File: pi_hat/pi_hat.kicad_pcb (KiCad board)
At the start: 2 copper layers, 65 x 56.5 mm, 47 parts, among them J1 Conn_Coaxial, J2 Conn_Coaxial, J3 Conn_02x20_Odd_Even, J4 Conn_02x04_Odd_Even, J5 Conn_02x02_Odd_Even, T1 2873002402, T2 2873002402, U1 FOX924, U2 Si5351A-B-GM, U3 FST3253, U4 FST3253, U5 TLV320ADC5140, U6 CAT24C32

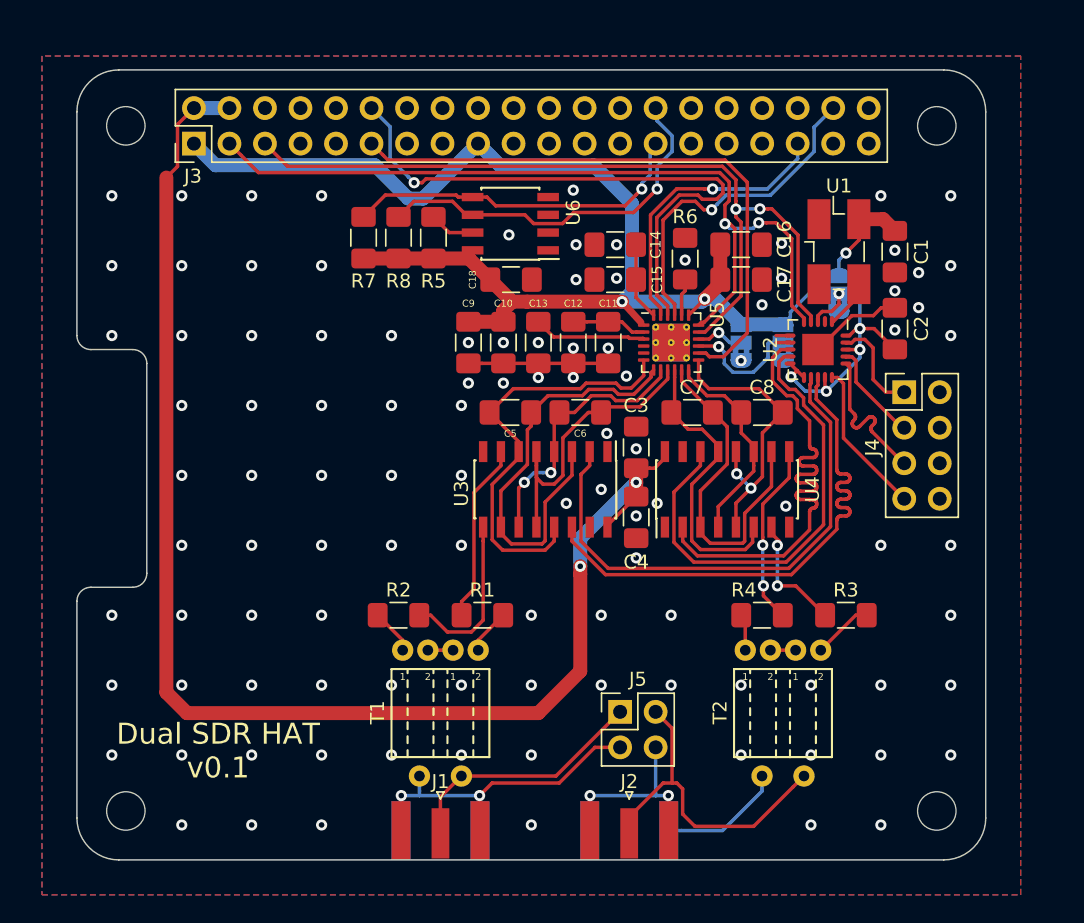
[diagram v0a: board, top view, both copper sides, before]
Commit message: Add header for external filter board
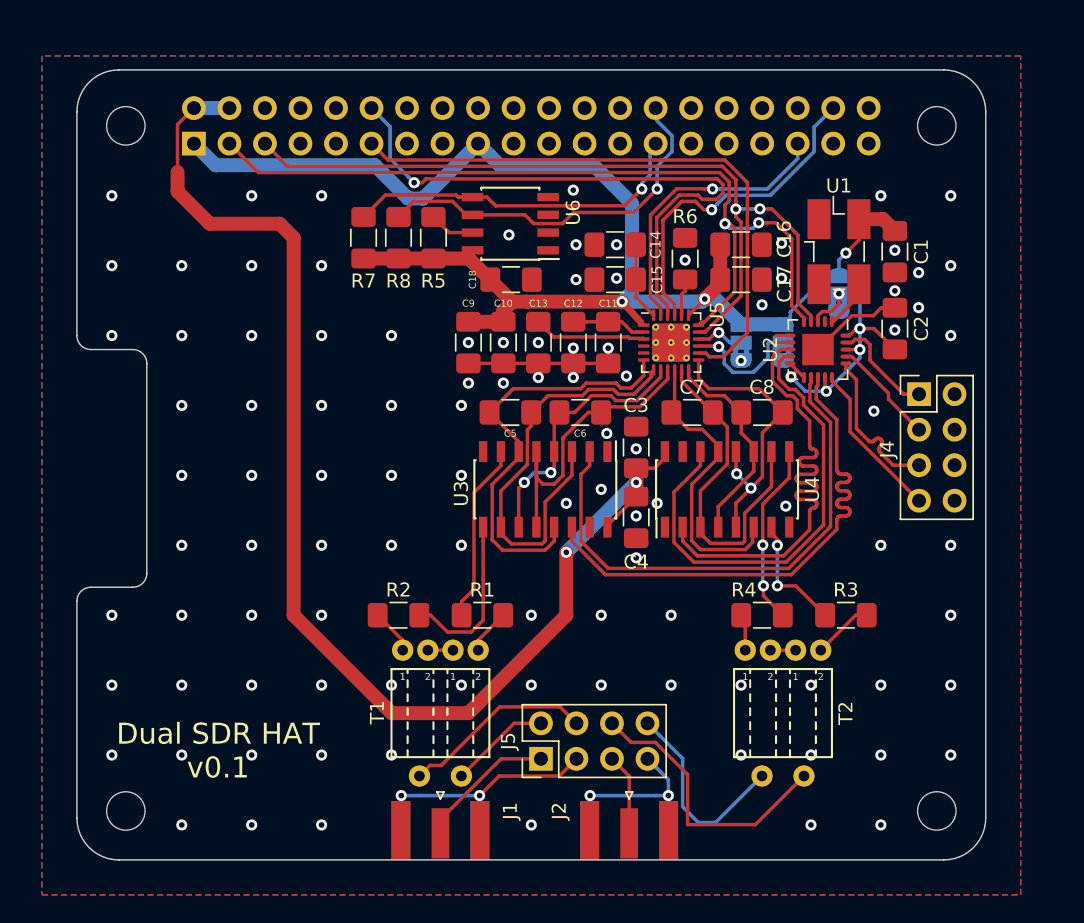
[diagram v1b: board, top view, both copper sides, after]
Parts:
- removed REF** (x4): MountingHole_2.7mm_M2.5, MountingHole:MountingHole_2.7mm_M2.5
- removed REF**: Slot_2.0x17.0mm, Bitglue:Slot_2.0x17.0mm
- J3: footprint Connector_PinHeader_2.54mm:PinHeader_2x20_P2.54mm_Vertical -> Bitglue:Pi_HAT
- J5: value Conn_02x02_Odd_Even -> Conn_02x04_Odd_Even; footprint Connector_PinHeader_2.54mm:PinHeader_2x02_P2.54mm_Vertical -> Connector_PinHeader_2.54mm:PinHeader_2x04_P2.54mm_Vertical
- moved J3 51.9 mm to (107.0, 129.0), turned to 0 degrees
- moved J5 6.58 mm to (140.2, 121.8), turned to 90 degrees
- moved J4 1.07 mm to (167.2, 95.7)
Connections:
- J5 pad 2: Net-(J2-Pad1) -> Net-(J5-Pad2)
- J5 pad 4: Net-(J2-Pad2) -> Net-(J5-Pad4)
- T1 pad 1: Net-(J1-Pad1) -> Net-(J5-Pad2)
- T1 pad 2: Net-(J1-Pad2) -> Net-(J5-Pad4)
- T2 pad 1: Net-(J2-Pad1) -> Net-(J5-Pad6)
- T2 pad 2: Net-(J2-Pad2) -> Net-(J5-Pad8)
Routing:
- net Net-(J5-Pad6): track 0.00 -> 20.3 mm
- net Net-(J2-Pad1): track 24.1 -> 5.84 mm
- net Net-(J5-Pad8): track 0.00 -> 14.5 mm
- net Net-(J5-Pad4): track 0.00 -> 13.8 mm
- net +5V: track 99.6 -> 90.4 mm
- net Net-(J2-Pad2): track 28.0 -> 18.9 mm
- net Net-(J1-Pad1): track 18.0 -> 9.98 mm
- net Net-(J5-Pad2): track 0.00 -> 7.25 mm
- net Net-(J1-Pad2): track 28.5 -> 23.7 mm
- net GND: vias 106 -> 104

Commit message: Add additional decoupling capacitors
Si5351 datasheet says we need one per supply pin.

Also added a couple caps right at the Pi header. Seemed like a good idea
to limit noise coming on to the board.
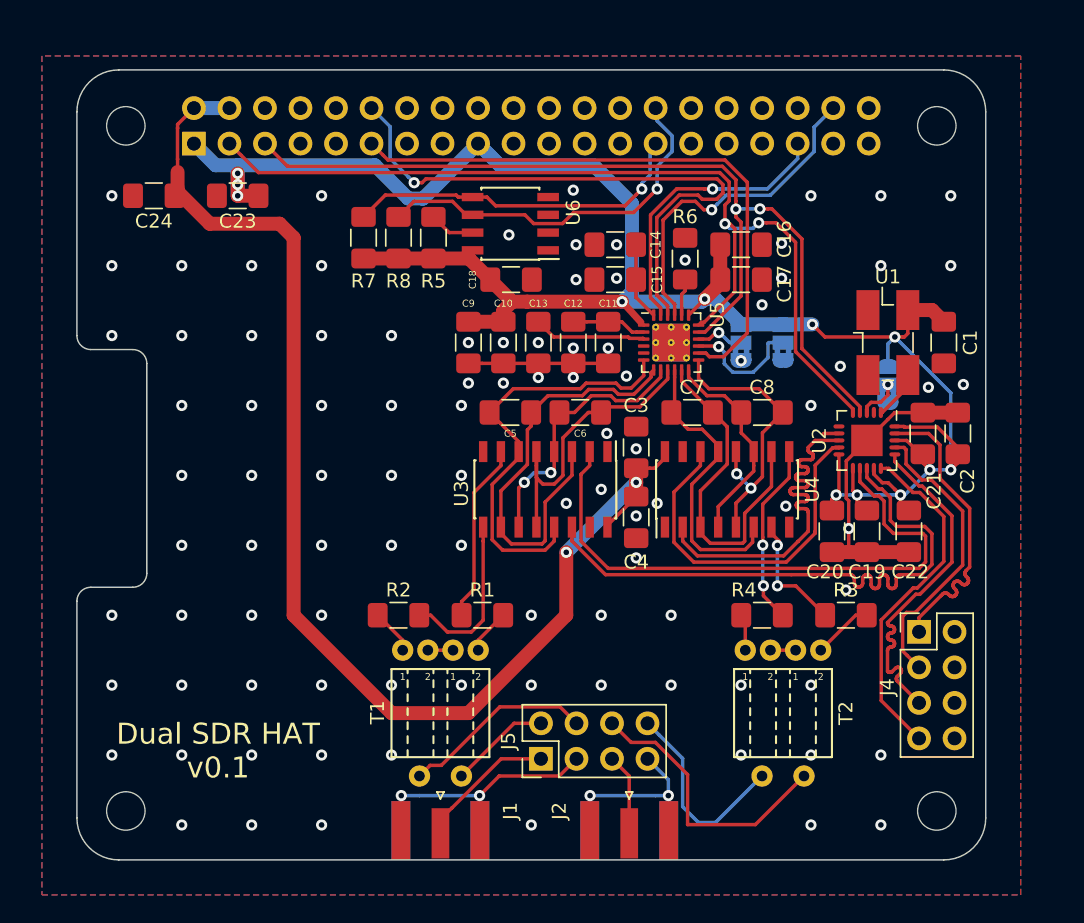
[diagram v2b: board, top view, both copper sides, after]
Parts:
- added C19: 0.1u, Capacitor_SMD:C_1206_3216Metric_Pad1.42x1.75mm_HandSolder, F.Cu at (163.5, 105.5)
- added C20: 0.1u, Capacitor_SMD:C_1206_3216Metric_Pad1.42x1.75mm_HandSolder, F.Cu at (161.0, 105.5)
- added C21: 0.1u, Capacitor_SMD:C_1206_3216Metric_Pad1.42x1.75mm_HandSolder, F.Cu at (167.5, 98.5)
- added C22: 0.1u, Capacitor_SMD:C_1206_3216Metric_Pad1.42x1.75mm_HandSolder, F.Cu at (166.5, 105.5)
- added C23: 1u, Capacitor_SMD:C_1206_3216Metric_Pad1.42x1.75mm_HandSolder, F.Cu at (118.5, 81.5)
- added C24: 1u, Capacitor_SMD:C_1206_3216Metric_Pad1.42x1.75mm_HandSolder, F.Cu at (112.5, 81.5)
- moved J4 17.0 mm to (167.2, 112.7)
- moved C2 8.75 mm to (170.0, 98.5)
- moved C1 7.38 mm to (169.0, 92.0)
- moved JP1 7.38 mm to (165.0, 95.0)
- moved U1 7.38 mm to (165.0, 92.0)
- moved U2 7.38 mm to (163.5, 99.0)
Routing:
- net +3V3: track 124.1 -> 154.5 mm, vias 7 -> 12
- net GND: track 19.1 -> 32.9 mm, vias 104 -> 98
- net /CLK4+: track 11.4 -> 24.9 mm
- net /CLK4-: track 11.4 -> 24.9 mm
- net /CLK3+: track 7.61 -> 21.2 mm
- net /CLK3-: track 7.64 -> 21.2 mm
- net /CLK2-: track 33.9 -> 25.9 mm
- net /SDA: track 60.8 -> 68.7 mm
- net /SCL: track 59.1 -> 67.1 mm
- net /CLK2+: track 33.8 -> 25.9 mm
- net /CLK1-: track 37.9 -> 42.4 mm
- net /CLK1+: track 37.9 -> 42.4 mm
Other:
- rule trace_min: 0.2 -> 0.1524
- rule via_min_drill: 0.3 -> 0.254
- rule via_min_size: 0.4 -> 0.508

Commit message: Improve layout after review
- Move I2C lines from under decoupling cap
- Beef up power supply traces and add more vias
- Add another 3.3V bypass cap near the header

Also, added a .100" grid of plated holes in the unused area, because why
not.
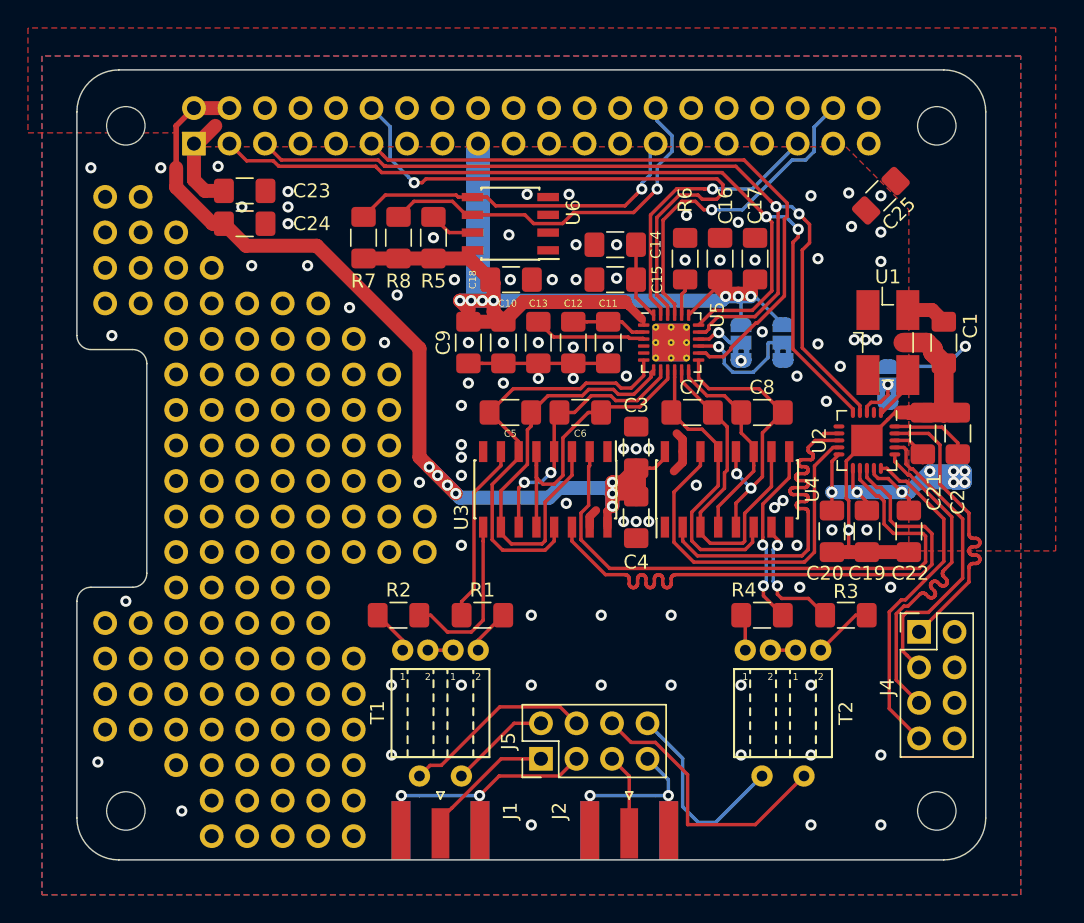
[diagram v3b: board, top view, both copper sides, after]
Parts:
- added C25: 1u, Capacitor_SMD:C_1206_3216Metric_Pad1.42x1.75mm_HandSolder, F.Cu at (164.5, 81.5)
- added REF**: THT_Pin_D1.7mm_Drill1.0mm, Bitglue:THT_Pin_D1.7mm_Drill1.0mm, F.Cu at (109.0, 112.1)
- added REF**: THT_Pin_D1.7mm_Drill1.0mm, Bitglue:THT_Pin_D1.7mm_Drill1.0mm, F.Cu at (131.9, 104.4)
- added REF**: THT_Pin_D1.7mm_Drill1.0mm, Bitglue:THT_Pin_D1.7mm_Drill1.0mm, F.Cu at (116.6, 91.7)
- added REF**: THT_Pin_D1.7mm_Drill1.0mm, Bitglue:THT_Pin_D1.7mm_Drill1.0mm, F.Cu at (114.1, 94.3)
- added REF**: THT_Pin_D1.7mm_Drill1.0mm, Bitglue:THT_Pin_D1.7mm_Drill1.0mm, F.Cu at (121.7, 94.3)
- added REF**: THT_Pin_D1.7mm_Drill1.0mm, Bitglue:THT_Pin_D1.7mm_Drill1.0mm, F.Cu at (121.7, 99.4)
- added REF**: THT_Pin_D1.7mm_Drill1.0mm, Bitglue:THT_Pin_D1.7mm_Drill1.0mm, F.Cu at (116.6, 96.8)
- added REF**: THT_Pin_D1.7mm_Drill1.0mm, Bitglue:THT_Pin_D1.7mm_Drill1.0mm, F.Cu at (114.1, 99.4)
- added REF**: THT_Pin_D1.7mm_Drill1.0mm, Bitglue:THT_Pin_D1.7mm_Drill1.0mm, F.Cu at (119.2, 96.8)
- added REF**: THT_Pin_D1.7mm_Drill1.0mm, Bitglue:THT_Pin_D1.7mm_Drill1.0mm, F.Cu at (119.2, 99.4)
- added REF**: THT_Pin_D1.7mm_Drill1.0mm, Bitglue:THT_Pin_D1.7mm_Drill1.0mm, F.Cu at (121.7, 96.8)
- added REF**: THT_Pin_D1.7mm_Drill1.0mm, Bitglue:THT_Pin_D1.7mm_Drill1.0mm, F.Cu at (114.1, 96.8)
- added REF**: THT_Pin_D1.7mm_Drill1.0mm, Bitglue:THT_Pin_D1.7mm_Drill1.0mm, F.Cu at (129.3, 107.0)
- added REF**: THT_Pin_D1.7mm_Drill1.0mm, Bitglue:THT_Pin_D1.7mm_Drill1.0mm, F.Cu at (116.6, 99.4)
- added REF**: THT_Pin_D1.7mm_Drill1.0mm, Bitglue:THT_Pin_D1.7mm_Drill1.0mm, F.Cu at (116.6, 104.4)
- added REF**: THT_Pin_D1.7mm_Drill1.0mm, Bitglue:THT_Pin_D1.7mm_Drill1.0mm, F.Cu at (114.1, 101.9)
- added REF**: THT_Pin_D1.7mm_Drill1.0mm, Bitglue:THT_Pin_D1.7mm_Drill1.0mm, F.Cu at (114.1, 104.4)
- added REF**: THT_Pin_D1.7mm_Drill1.0mm, Bitglue:THT_Pin_D1.7mm_Drill1.0mm, F.Cu at (116.6, 101.9)
- added REF**: THT_Pin_D1.7mm_Drill1.0mm, Bitglue:THT_Pin_D1.7mm_Drill1.0mm, F.Cu at (121.7, 101.9)
- added REF**: THT_Pin_D1.7mm_Drill1.0mm, Bitglue:THT_Pin_D1.7mm_Drill1.0mm, F.Cu at (119.2, 101.9)
- added REF**: THT_Pin_D1.7mm_Drill1.0mm, Bitglue:THT_Pin_D1.7mm_Drill1.0mm, F.Cu at (121.7, 104.4)
- added REF**: THT_Pin_D1.7mm_Drill1.0mm, Bitglue:THT_Pin_D1.7mm_Drill1.0mm, F.Cu at (119.2, 104.4)
- added REF**: THT_Pin_D1.7mm_Drill1.0mm, Bitglue:THT_Pin_D1.7mm_Drill1.0mm, F.Cu at (129.3, 104.4)
- added REF**: THT_Pin_D1.7mm_Drill1.0mm, Bitglue:THT_Pin_D1.7mm_Drill1.0mm, F.Cu at (129.3, 99.4)
- added REF**: THT_Pin_D1.7mm_Drill1.0mm, Bitglue:THT_Pin_D1.7mm_Drill1.0mm, F.Cu at (129.3, 96.8)
- added REF**: THT_Pin_D1.7mm_Drill1.0mm, Bitglue:THT_Pin_D1.7mm_Drill1.0mm, F.Cu at (129.3, 94.3)
- added REF**: THT_Pin_D1.7mm_Drill1.0mm, Bitglue:THT_Pin_D1.7mm_Drill1.0mm, F.Cu at (129.3, 101.9)
- added REF**: THT_Pin_D1.7mm_Drill1.0mm, Bitglue:THT_Pin_D1.7mm_Drill1.0mm, F.Cu at (114.1, 84.1)
- added REF**: THT_Pin_D1.7mm_Drill1.0mm, Bitglue:THT_Pin_D1.7mm_Drill1.0mm, F.Cu at (111.6, 81.6)
- added REF**: THT_Pin_D1.7mm_Drill1.0mm, Bitglue:THT_Pin_D1.7mm_Drill1.0mm, F.Cu at (109.0, 81.6)
- added REF**: THT_Pin_D1.7mm_Drill1.0mm, Bitglue:THT_Pin_D1.7mm_Drill1.0mm, F.Cu at (109.0, 119.7)
- added REF**: THT_Pin_D1.7mm_Drill1.0mm, Bitglue:THT_Pin_D1.7mm_Drill1.0mm, F.Cu at (109.0, 84.1)
- added REF**: THT_Pin_D1.7mm_Drill1.0mm, Bitglue:THT_Pin_D1.7mm_Drill1.0mm, F.Cu at (111.6, 84.1)
- added REF**: THT_Pin_D1.7mm_Drill1.0mm, Bitglue:THT_Pin_D1.7mm_Drill1.0mm, F.Cu at (126.8, 117.1)
- added REF**: THT_Pin_D1.7mm_Drill1.0mm, Bitglue:THT_Pin_D1.7mm_Drill1.0mm, F.Cu at (126.8, 101.9)
- added REF**: THT_Pin_D1.7mm_Drill1.0mm, Bitglue:THT_Pin_D1.7mm_Drill1.0mm, F.Cu at (126.8, 91.7)
- added REF**: THT_Pin_D1.7mm_Drill1.0mm, Bitglue:THT_Pin_D1.7mm_Drill1.0mm, F.Cu at (126.8, 124.8)
- added REF**: THT_Pin_D1.7mm_Drill1.0mm, Bitglue:THT_Pin_D1.7mm_Drill1.0mm, F.Cu at (126.8, 107.0)
- added REF**: THT_Pin_D1.7mm_Drill1.0mm, Bitglue:THT_Pin_D1.7mm_Drill1.0mm, F.Cu at (126.8, 99.4)
- added REF**: THT_Pin_D1.7mm_Drill1.0mm, Bitglue:THT_Pin_D1.7mm_Drill1.0mm, F.Cu at (126.8, 114.6)
- added REF**: THT_Pin_D1.7mm_Drill1.0mm, Bitglue:THT_Pin_D1.7mm_Drill1.0mm, F.Cu at (126.8, 127.3)
- added REF**: THT_Pin_D1.7mm_Drill1.0mm, Bitglue:THT_Pin_D1.7mm_Drill1.0mm, F.Cu at (109.0, 114.6)
- added REF**: THT_Pin_D1.7mm_Drill1.0mm, Bitglue:THT_Pin_D1.7mm_Drill1.0mm, F.Cu at (126.8, 94.3)
- added REF**: THT_Pin_D1.7mm_Drill1.0mm, Bitglue:THT_Pin_D1.7mm_Drill1.0mm, F.Cu at (126.8, 122.2)
- added REF**: THT_Pin_D1.7mm_Drill1.0mm, Bitglue:THT_Pin_D1.7mm_Drill1.0mm, F.Cu at (126.8, 96.8)
- added REF**: THT_Pin_D1.7mm_Drill1.0mm, Bitglue:THT_Pin_D1.7mm_Drill1.0mm, F.Cu at (126.8, 104.4)
- added REF**: THT_Pin_D1.7mm_Drill1.0mm, Bitglue:THT_Pin_D1.7mm_Drill1.0mm, F.Cu at (126.8, 119.7)
- added REF**: THT_Pin_D1.7mm_Drill1.0mm, Bitglue:THT_Pin_D1.7mm_Drill1.0mm, F.Cu at (124.3, 96.8)
- added REF**: THT_Pin_D1.7mm_Drill1.0mm, Bitglue:THT_Pin_D1.7mm_Drill1.0mm, F.Cu at (124.3, 104.4)
- added REF**: THT_Pin_D1.7mm_Drill1.0mm, Bitglue:THT_Pin_D1.7mm_Drill1.0mm, F.Cu at (124.3, 109.5)
- added REF**: THT_Pin_D1.7mm_Drill1.0mm, Bitglue:THT_Pin_D1.7mm_Drill1.0mm, F.Cu at (124.3, 122.2)
- added REF**: THT_Pin_D1.7mm_Drill1.0mm, Bitglue:THT_Pin_D1.7mm_Drill1.0mm, F.Cu at (124.3, 89.2)
- added REF**: THT_Pin_D1.7mm_Drill1.0mm, Bitglue:THT_Pin_D1.7mm_Drill1.0mm, F.Cu at (109.0, 117.1)
- added REF**: THT_Pin_D1.7mm_Drill1.0mm, Bitglue:THT_Pin_D1.7mm_Drill1.0mm, F.Cu at (124.3, 112.1)
- added REF**: THT_Pin_D1.7mm_Drill1.0mm, Bitglue:THT_Pin_D1.7mm_Drill1.0mm, F.Cu at (124.3, 119.7)
- added REF**: THT_Pin_D1.7mm_Drill1.0mm, Bitglue:THT_Pin_D1.7mm_Drill1.0mm, F.Cu at (124.3, 94.3)
- added REF**: THT_Pin_D1.7mm_Drill1.0mm, Bitglue:THT_Pin_D1.7mm_Drill1.0mm, F.Cu at (124.3, 127.3)
- added REF**: THT_Pin_D1.7mm_Drill1.0mm, Bitglue:THT_Pin_D1.7mm_Drill1.0mm, F.Cu at (124.3, 101.9)
- added REF**: THT_Pin_D1.7mm_Drill1.0mm, Bitglue:THT_Pin_D1.7mm_Drill1.0mm, F.Cu at (124.3, 91.7)
- added REF**: THT_Pin_D1.7mm_Drill1.0mm, Bitglue:THT_Pin_D1.7mm_Drill1.0mm, F.Cu at (124.3, 117.1)
- added REF**: THT_Pin_D1.7mm_Drill1.0mm, Bitglue:THT_Pin_D1.7mm_Drill1.0mm, F.Cu at (124.3, 99.4)
- added REF**: THT_Pin_D1.7mm_Drill1.0mm, Bitglue:THT_Pin_D1.7mm_Drill1.0mm, F.Cu at (124.3, 114.6)
- added REF**: THT_Pin_D1.7mm_Drill1.0mm, Bitglue:THT_Pin_D1.7mm_Drill1.0mm, F.Cu at (124.3, 107.0)
- added REF**: THT_Pin_D1.7mm_Drill1.0mm, Bitglue:THT_Pin_D1.7mm_Drill1.0mm, F.Cu at (111.6, 119.7)
- added REF**: THT_Pin_D1.7mm_Drill1.0mm, Bitglue:THT_Pin_D1.7mm_Drill1.0mm, F.Cu at (124.3, 124.8)
- added REF**: THT_Pin_D1.7mm_Drill1.0mm, Bitglue:THT_Pin_D1.7mm_Drill1.0mm, F.Cu at (119.2, 89.2)
- added REF**: THT_Pin_D1.7mm_Drill1.0mm, Bitglue:THT_Pin_D1.7mm_Drill1.0mm, F.Cu at (121.7, 89.2)
- added REF**: THT_Pin_D1.7mm_Drill1.0mm, Bitglue:THT_Pin_D1.7mm_Drill1.0mm, F.Cu at (116.6, 127.3)
- added REF**: THT_Pin_D1.7mm_Drill1.0mm, Bitglue:THT_Pin_D1.7mm_Drill1.0mm, F.Cu at (119.2, 127.3)
- added REF**: THT_Pin_D1.7mm_Drill1.0mm, Bitglue:THT_Pin_D1.7mm_Drill1.0mm, F.Cu at (121.7, 127.3)
- added REF**: THT_Pin_D1.7mm_Drill1.0mm, Bitglue:THT_Pin_D1.7mm_Drill1.0mm, F.Cu at (116.6, 122.2)
- added REF**: THT_Pin_D1.7mm_Drill1.0mm, Bitglue:THT_Pin_D1.7mm_Drill1.0mm, F.Cu at (119.2, 122.2)
- added REF**: THT_Pin_D1.7mm_Drill1.0mm, Bitglue:THT_Pin_D1.7mm_Drill1.0mm, F.Cu at (121.7, 124.8)
- added REF**: THT_Pin_D1.7mm_Drill1.0mm, Bitglue:THT_Pin_D1.7mm_Drill1.0mm, F.Cu at (114.1, 122.2)
- added REF**: THT_Pin_D1.7mm_Drill1.0mm, Bitglue:THT_Pin_D1.7mm_Drill1.0mm, F.Cu at (111.6, 117.1)
- added REF**: THT_Pin_D1.7mm_Drill1.0mm, Bitglue:THT_Pin_D1.7mm_Drill1.0mm, F.Cu at (121.7, 122.2)
- added REF**: THT_Pin_D1.7mm_Drill1.0mm, Bitglue:THT_Pin_D1.7mm_Drill1.0mm, F.Cu at (116.6, 124.8)
- added REF**: THT_Pin_D1.7mm_Drill1.0mm, Bitglue:THT_Pin_D1.7mm_Drill1.0mm, F.Cu at (119.2, 124.8)
- added REF**: THT_Pin_D1.7mm_Drill1.0mm, Bitglue:THT_Pin_D1.7mm_Drill1.0mm, F.Cu at (116.6, 119.7)
- added REF**: THT_Pin_D1.7mm_Drill1.0mm, Bitglue:THT_Pin_D1.7mm_Drill1.0mm, F.Cu at (119.2, 119.7)
- added REF**: THT_Pin_D1.7mm_Drill1.0mm, Bitglue:THT_Pin_D1.7mm_Drill1.0mm, F.Cu at (121.7, 117.1)
- added REF**: THT_Pin_D1.7mm_Drill1.0mm, Bitglue:THT_Pin_D1.7mm_Drill1.0mm, F.Cu at (114.1, 117.1)
- added REF**: THT_Pin_D1.7mm_Drill1.0mm, Bitglue:THT_Pin_D1.7mm_Drill1.0mm, F.Cu at (121.7, 119.7)
- added REF**: THT_Pin_D1.7mm_Drill1.0mm, Bitglue:THT_Pin_D1.7mm_Drill1.0mm, F.Cu at (119.2, 117.1)
- added REF**: THT_Pin_D1.7mm_Drill1.0mm, Bitglue:THT_Pin_D1.7mm_Drill1.0mm, F.Cu at (114.1, 119.7)
- added REF**: THT_Pin_D1.7mm_Drill1.0mm, Bitglue:THT_Pin_D1.7mm_Drill1.0mm, F.Cu at (111.6, 114.6)
- added REF**: THT_Pin_D1.7mm_Drill1.0mm, Bitglue:THT_Pin_D1.7mm_Drill1.0mm, F.Cu at (116.6, 117.1)
- added REF**: THT_Pin_D1.7mm_Drill1.0mm, Bitglue:THT_Pin_D1.7mm_Drill1.0mm, F.Cu at (121.7, 114.6)
- added REF**: THT_Pin_D1.7mm_Drill1.0mm, Bitglue:THT_Pin_D1.7mm_Drill1.0mm, F.Cu at (119.2, 112.1)
- added REF**: THT_Pin_D1.7mm_Drill1.0mm, Bitglue:THT_Pin_D1.7mm_Drill1.0mm, F.Cu at (114.1, 114.6)
- added REF**: THT_Pin_D1.7mm_Drill1.0mm, Bitglue:THT_Pin_D1.7mm_Drill1.0mm, F.Cu at (116.6, 112.1)
- added REF**: THT_Pin_D1.7mm_Drill1.0mm, Bitglue:THT_Pin_D1.7mm_Drill1.0mm, F.Cu at (121.7, 112.1)
- added REF**: THT_Pin_D1.7mm_Drill1.0mm, Bitglue:THT_Pin_D1.7mm_Drill1.0mm, F.Cu at (119.2, 114.6)
- added REF**: THT_Pin_D1.7mm_Drill1.0mm, Bitglue:THT_Pin_D1.7mm_Drill1.0mm, F.Cu at (114.1, 112.1)
- added REF**: THT_Pin_D1.7mm_Drill1.0mm, Bitglue:THT_Pin_D1.7mm_Drill1.0mm, F.Cu at (116.6, 114.6)
- added REF**: THT_Pin_D1.7mm_Drill1.0mm, Bitglue:THT_Pin_D1.7mm_Drill1.0mm, F.Cu at (116.6, 109.5)
- added REF**: THT_Pin_D1.7mm_Drill1.0mm, Bitglue:THT_Pin_D1.7mm_Drill1.0mm, F.Cu at (111.6, 112.1)
- added REF**: THT_Pin_D1.7mm_Drill1.0mm, Bitglue:THT_Pin_D1.7mm_Drill1.0mm, F.Cu at (121.7, 107.0)
- added REF**: THT_Pin_D1.7mm_Drill1.0mm, Bitglue:THT_Pin_D1.7mm_Drill1.0mm, F.Cu at (114.1, 107.0)
- added REF**: THT_Pin_D1.7mm_Drill1.0mm, Bitglue:THT_Pin_D1.7mm_Drill1.0mm, F.Cu at (119.2, 109.5)
- added REF**: THT_Pin_D1.7mm_Drill1.0mm, Bitglue:THT_Pin_D1.7mm_Drill1.0mm, F.Cu at (114.1, 109.5)
- added REF**: THT_Pin_D1.7mm_Drill1.0mm, Bitglue:THT_Pin_D1.7mm_Drill1.0mm, F.Cu at (119.2, 107.0)
- added REF**: THT_Pin_D1.7mm_Drill1.0mm, Bitglue:THT_Pin_D1.7mm_Drill1.0mm, F.Cu at (121.7, 109.5)
- added REF**: THT_Pin_D1.7mm_Drill1.0mm, Bitglue:THT_Pin_D1.7mm_Drill1.0mm, F.Cu at (116.6, 107.0)
- added REF**: THT_Pin_D1.7mm_Drill1.0mm, Bitglue:THT_Pin_D1.7mm_Drill1.0mm, F.Cu at (111.6, 86.7)
- added REF**: THT_Pin_D1.7mm_Drill1.0mm, Bitglue:THT_Pin_D1.7mm_Drill1.0mm, F.Cu at (114.1, 86.7)
- added REF**: THT_Pin_D1.7mm_Drill1.0mm, Bitglue:THT_Pin_D1.7mm_Drill1.0mm, F.Cu at (109.0, 89.2)
- added REF**: THT_Pin_D1.7mm_Drill1.0mm, Bitglue:THT_Pin_D1.7mm_Drill1.0mm, F.Cu at (131.9, 107.0)
- added REF**: THT_Pin_D1.7mm_Drill1.0mm, Bitglue:THT_Pin_D1.7mm_Drill1.0mm, F.Cu at (116.6, 89.2)
- added REF**: THT_Pin_D1.7mm_Drill1.0mm, Bitglue:THT_Pin_D1.7mm_Drill1.0mm, F.Cu at (109.0, 86.7)
- added REF**: THT_Pin_D1.7mm_Drill1.0mm, Bitglue:THT_Pin_D1.7mm_Drill1.0mm, F.Cu at (116.6, 86.7)
- added REF**: THT_Pin_D1.7mm_Drill1.0mm, Bitglue:THT_Pin_D1.7mm_Drill1.0mm, F.Cu at (111.6, 89.2)
- added REF**: THT_Pin_D1.7mm_Drill1.0mm, Bitglue:THT_Pin_D1.7mm_Drill1.0mm, F.Cu at (114.1, 89.2)
- added REF**: THT_Pin_D1.7mm_Drill1.0mm, Bitglue:THT_Pin_D1.7mm_Drill1.0mm, F.Cu at (114.1, 91.7)
- added REF**: THT_Pin_D1.7mm_Drill1.0mm, Bitglue:THT_Pin_D1.7mm_Drill1.0mm, F.Cu at (116.6, 94.3)
- added REF**: THT_Pin_D1.7mm_Drill1.0mm, Bitglue:THT_Pin_D1.7mm_Drill1.0mm, F.Cu at (121.7, 91.7)
- added REF**: THT_Pin_D1.7mm_Drill1.0mm, Bitglue:THT_Pin_D1.7mm_Drill1.0mm, F.Cu at (119.2, 94.3)
- added REF**: THT_Pin_D1.7mm_Drill1.0mm, Bitglue:THT_Pin_D1.7mm_Drill1.0mm, F.Cu at (119.2, 91.7)
- moved C24 6.80 mm to (119.0, 83.5), turned to 0 degrees
- moved C16 1.80 mm to (153.0, 86.0), turned to 90 degrees
- moved C17 1.80 mm to (155.5, 86.0), turned to 90 degrees
- moved C23 0.61 mm to (119.0, 81.2), turned to 0 degrees
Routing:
- net +3V3: track 154.5 -> 134.3 mm, vias 12 -> 16
- net +5V: track 90.4 -> 71.4 mm, vias 2 -> 7
- net GND: track 32.9 -> 44.3 mm, vias 98 -> 97
- net /SHDNZ: track 43.1 -> 46.3 mm
- net /SCL: track 67.1 -> 70.0 mm
- net /SDA: track 68.7 -> 70.0 mm
- net /CLK2-: track 25.9 -> 26.7 mm
- net /CLK2+: track 25.9 -> 26.7 mm
- net /LRCK: track 20.7 -> 20.1 mm
- net Net-(R3-Pad1): track 8.76 -> 9.36 mm
- net /CLK4+: track 24.9 -> 24.4 mm
- net /CLK4-: track 24.9 -> 24.4 mm
- added copper zone on F.Cu, net +3V3
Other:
- rule solder_mask_min_width: 0.25 -> 0.1016
